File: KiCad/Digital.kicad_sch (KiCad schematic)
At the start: 32 parts, among them J301 AVR-ISP-6, J302 USB B, U301 FT231XS-U, U302 ATMEGA328P-AUR, U303 ADuM261, U304 TMP117xxDRV, Y301 16 MHz

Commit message: Adjusted designators for NTCs
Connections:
- net TS1 renamed TSR
- net TS2 renamed TSM
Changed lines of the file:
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@@
     (effects (font (size 1.27 1.27)) (justify right bottom))
   )
-  (label "TS1" (at 45.085 130.81 0) (fields_autoplaced)
+  (label "TSR" (at 45.085 130.81 0) (fields_autoplaced)
     (effects (font (size 1.27 1.27)) (justify left bottom))
   )
@@
     (effects (font (size 1.27 1.27)) (justify right bottom))
   )
-  (label "TS2" (at 65.405 106.68 0) (fields_autoplaced)
+  (label "TSM" (at 65.405 106.68 0) (fields_autoplaced)
     (effects (font (size 1.27 1.27)) (justify left bottom))
   )
@@
     (effects (font (size 1.27 1.27)) (justify left bottom))
   )
-  (label "TS2" (at 45.085 142.24 0) (fields_autoplaced)
+  (label "TSM" (at 45.085 142.24 0) (fields_autoplaced)
     (effects (font (size 1.27 1.27)) (justify left bottom))
   )
@@
     (effects (font (size 1.27 1.27)) (justify right bottom))
   )
-  (label "TS1" (at 65.405 104.14 0) (fields_autoplaced)
+  (label "TSR" (at 65.405 104.14 0) (fields_autoplaced)
     (effects (font (size 1.27 1.27)) (justify left bottom))
   )

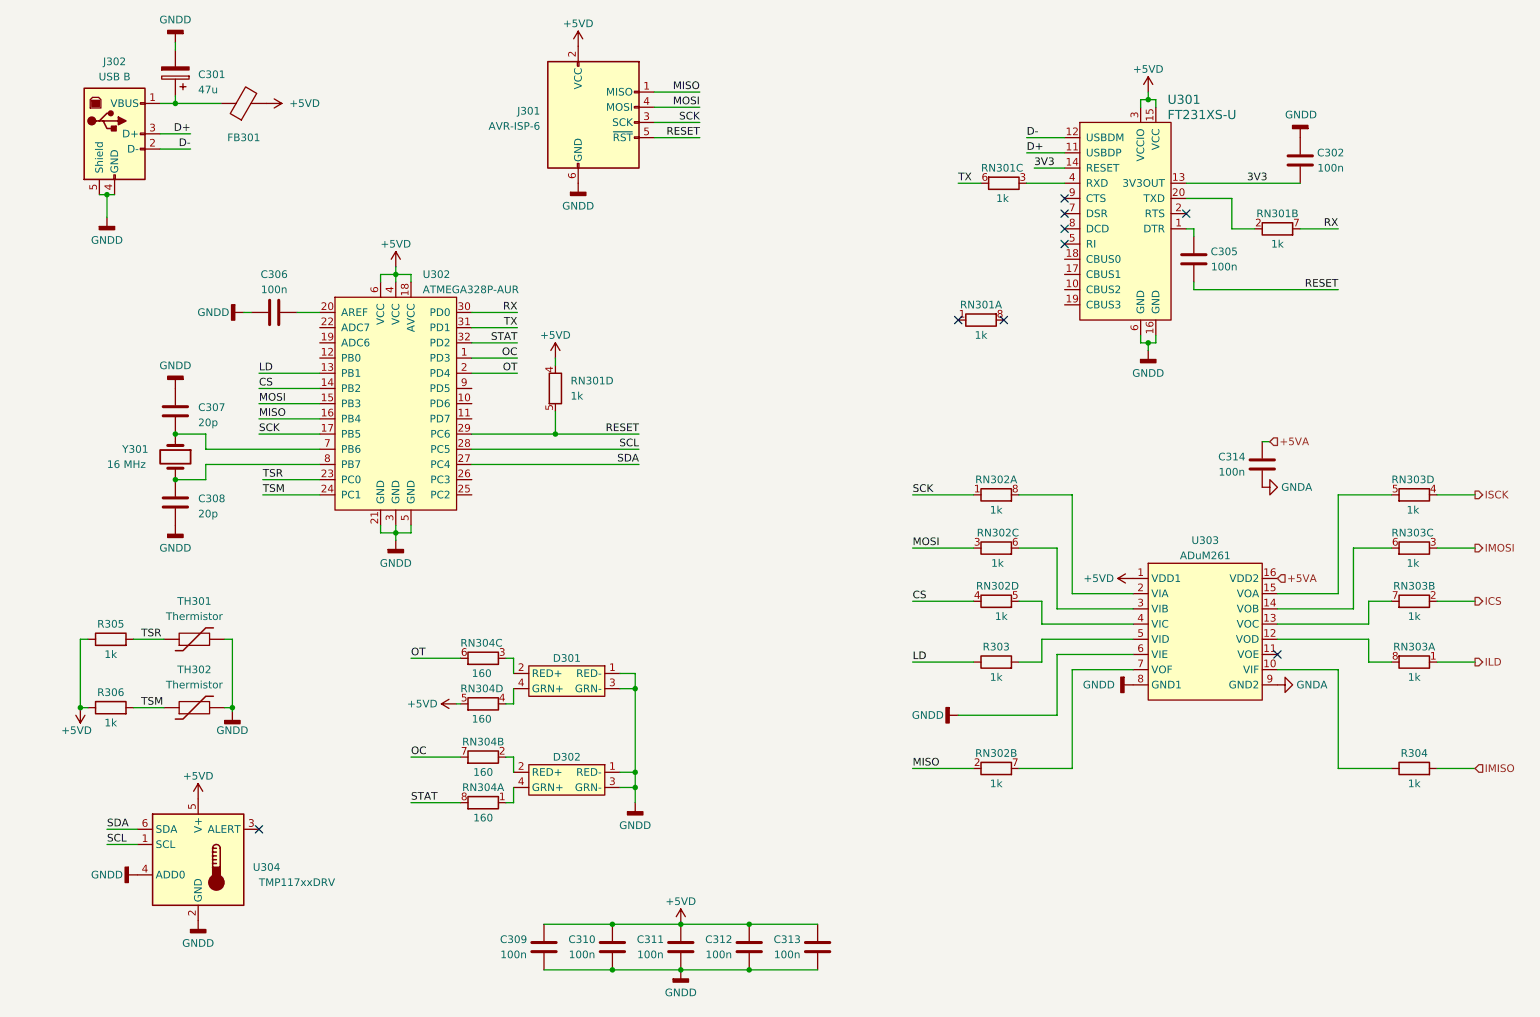
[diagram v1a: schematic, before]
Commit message: Updated some designators and added component list
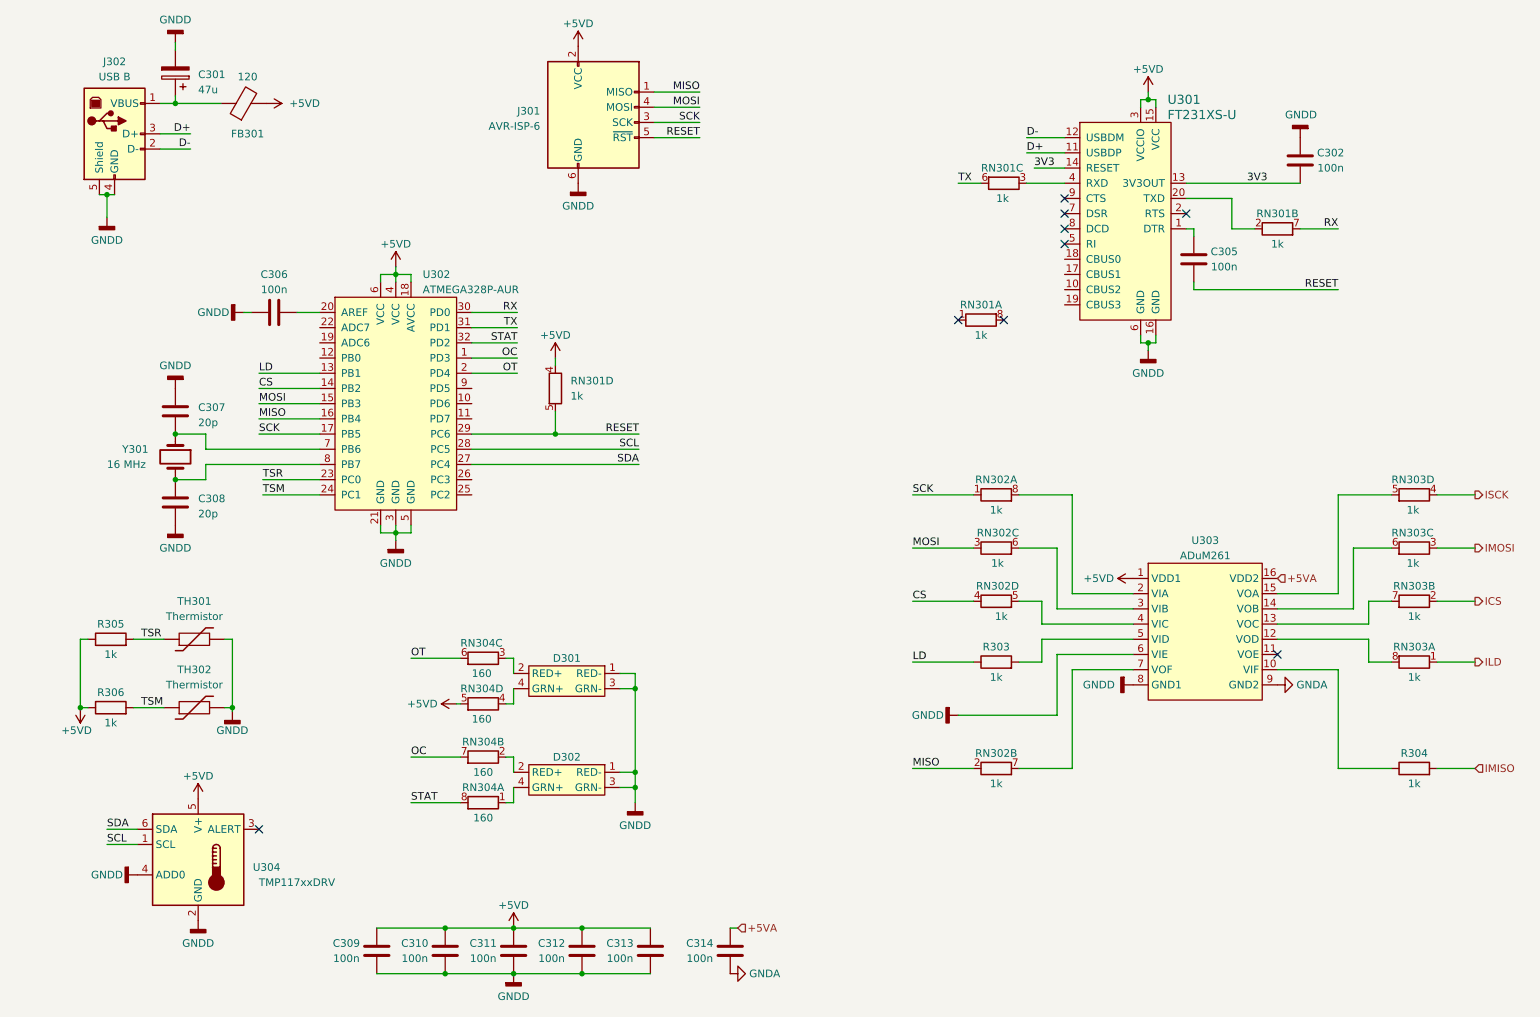
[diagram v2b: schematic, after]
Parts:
- FB301: value ~ -> 120
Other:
- moved on the sheet: C309, C310, C311, C312, C313, C314

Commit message: Cleaned up a few things
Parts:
- TH301, TH302: value Thermistor -> 1k
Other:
- note added: "BYPASS CAPS"
- note added: "INDICATOR LEDS"
- note added: "MICROCONTROLLER AND PROGRAMMING HEADER"
- note added: "OPTO-ISOLATOR"
- note added: "TEMPERATURE SENSORS"
- note added: "USB TO UART CONVERTER"
- company: Matt Morano -> M Morano
- title: Digital -> Precision Curernt Source Digital
- moved on the sheet: C306, C307, C308, C309, C310, C311, C312, C313, C314, D301, D302, J301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
